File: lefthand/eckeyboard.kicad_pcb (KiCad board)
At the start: 2 copper layers, 135.8 x 94.3 mm, 60 parts, among them J4 Conn_01x06_Male, J5 Conn_01x06_Male, U1 74HC4051, U2 NJM2742, U4 74LS138

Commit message: [add] controller, righthand
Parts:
- TP1, TP10, TP11, TP12, TP13, TP14, TP15, TP16, TP17, TP18, TP19, TP2, TP20, TP21, TP22, TP23, TP24, TP25, TP26, TP27, TP3, TP4, TP5, TP6, TP7, TP8, TP9: value ToprePad -> ToprePad_MntHole; footprint toprepad:ToprePad -> toprepad:ToprePad_MntHole
- moved C7 0.32 mm to (133.3, 129.9)
- moved R15 0.32 mm to (133.3, 131.5)
- moved C6 0.32 mm to (133.3, 126.8)
- moved R14 0.32 mm to (133.3, 128.3)
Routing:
- net GND: track 2927.1 -> 2891.3 mm, vias 9 -> 12
- net /ROW1: track 216.9 -> 227.5 mm
- net /ROW0: track 231.1 -> 238.4 mm
- net /ROW3: track 192.7 -> 199.8 mm
- net /ROW2: track 195.6 -> 198.9 mm
- net /COL3: track 149.5 -> 147.1 mm
- net /MUX_A: track 80.8 -> 82.7 mm
- net /READ: track 97.1 -> 98.3 mm
- net /COL4: track 141.3 -> 140.1 mm
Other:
- board size 135.8 x 94.3 mm -> 137.8 x 98.3 mm

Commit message: [add] step files
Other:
- outline, holes or cut-outs redrawn
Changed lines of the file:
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@@
   (general
     (thickness 1.6)
-    (drawings 47)
+    (drawings 46)
     (tracks 1324)
     (zones 0)
@@
     (arrow2b (pts (xy 31.75 38.95) (xy 32.336421 40.076504)))
   )
-  (gr_line (start 39 137.25) (end 41.05 137.25) (layer Edge.Cuts) (width 0.15))
   (gr_line (start 39 38.95) (end 39 137.25) (layer Edge.Cuts) (width 0.15))
   (gr_line (start 41 38.95) (end 39 38.95) (layer Edge.Cuts) (width 0.15))
@@
   (gr_line (start 176.8 116.65) (end 176.8 116.15) (layer Edge.Cuts) (width 0.15))
   (gr_line (start 167.8 116.65) (end 176.8 116.65) (layer Edge.Cuts) (width 0.15))
-  (gr_line (start 167.8 137.25) (end 41 137.25) (layer Edge.Cuts) (width 0.15))
+  (gr_line (start 167.8 137.25) (end 39 137.25) (layer Edge.Cuts) (width 0.15))
   (gr_line (start 167.8 135.2) (end 167.8 135.25) (layer Edge.Cuts) (width 0.15))
   (gr_line (start 167.8 137.25) (end 167.8 135.2) (layer Edge.Cuts) (width 0.15))

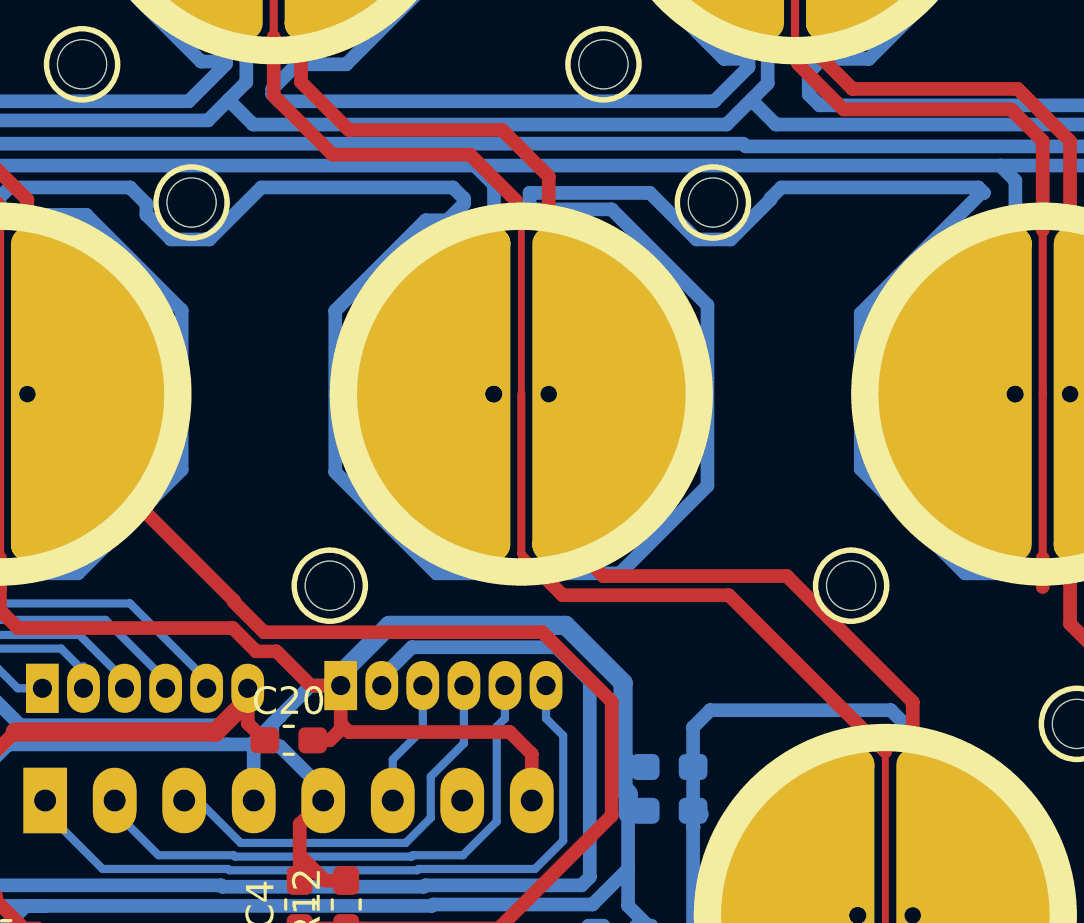
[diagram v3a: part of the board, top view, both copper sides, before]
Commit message: [fix] mounting hole conflict
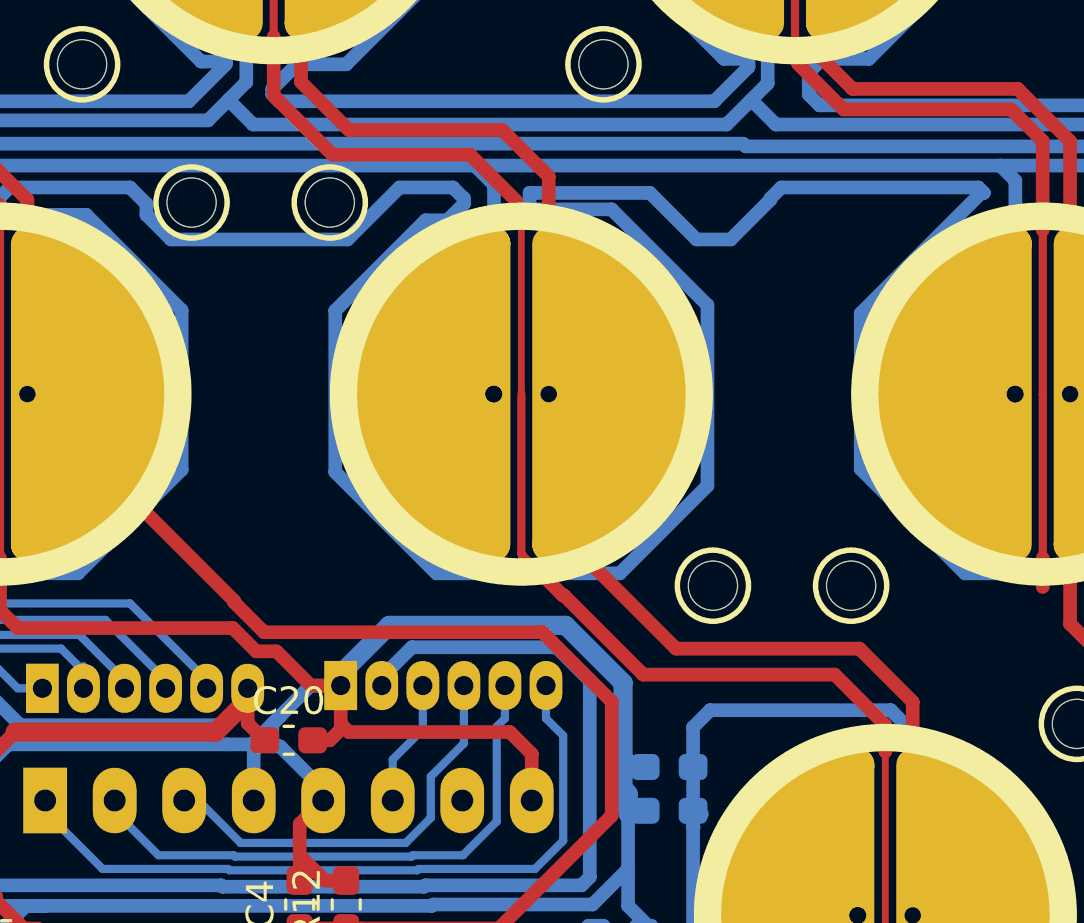
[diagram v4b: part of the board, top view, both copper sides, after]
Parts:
- TP18: value ToprePad_MntHole -> ToprePad_MntHole_B; footprint toprepad:ToprePad_MntHole -> toprepad:ToprePad_MntHole_B
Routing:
- net GND: track 2891.3 -> 2891.9 mm

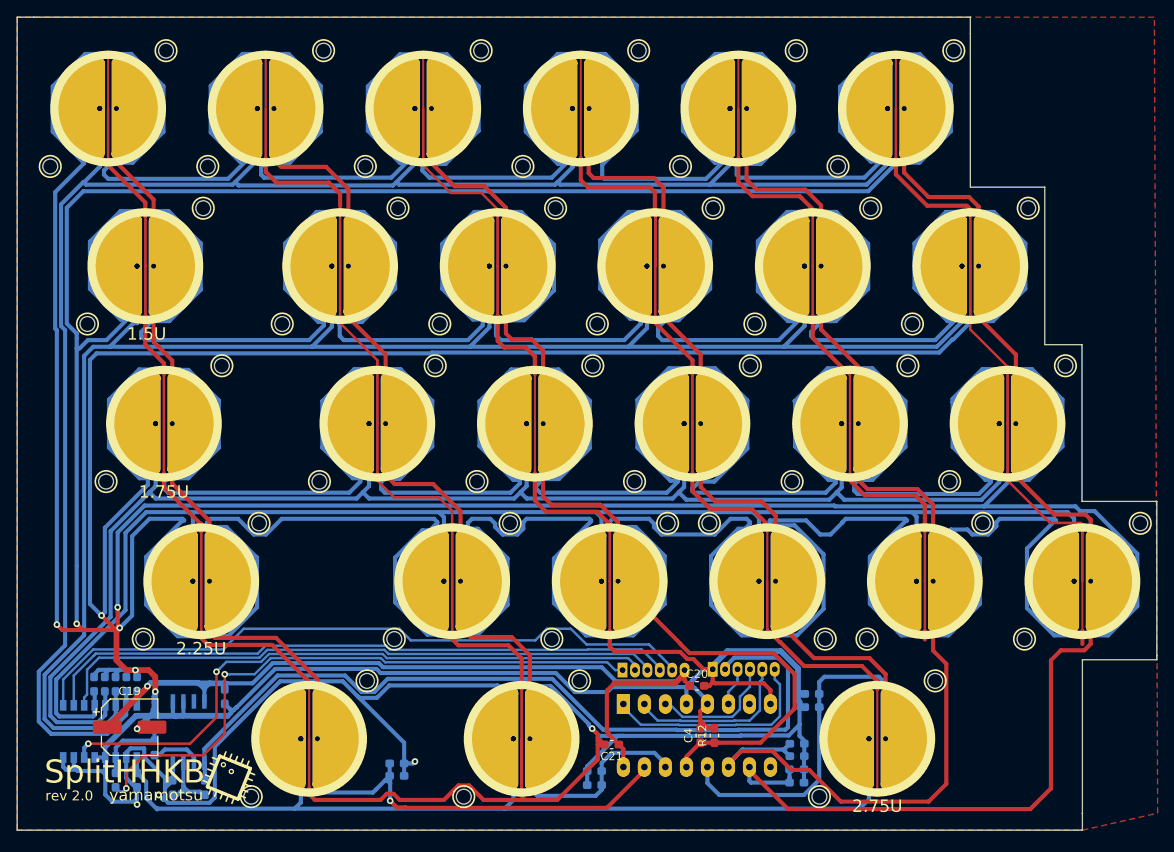
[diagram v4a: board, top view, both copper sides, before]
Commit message: [fix] MUX pin ordering fix
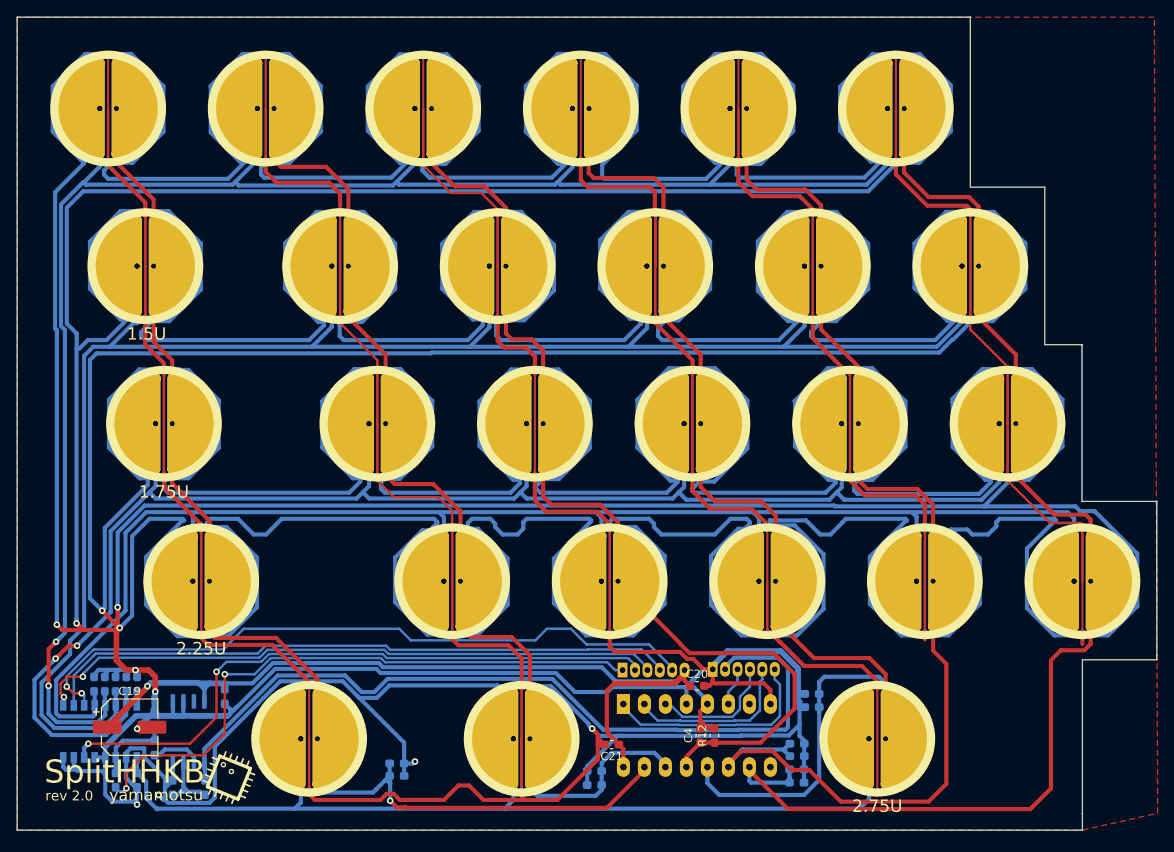
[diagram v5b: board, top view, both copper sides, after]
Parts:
- TP1, TP10, TP11, TP12, TP13, TP14, TP15, TP16, TP17, TP19, TP2, TP20, TP21, TP22, TP23, TP24, TP25, TP26, TP27, TP3, TP4, TP5, TP6, TP7, TP8, TP9: value ToprePad_MntHole -> ToprePad; footprint toprepad:ToprePad_MntHole -> toprepad:ToprePad
- TP18: value ToprePad_MntHole_B -> ToprePad; footprint toprepad:ToprePad_MntHole_B -> toprepad:ToprePad
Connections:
- R1 pad 1: /ROW2 -> /ROW0
- R3 pad 1: /ROW0 -> /ROW2
- U1 pad 11: /MUX_C -> /MUX_A
- U1 pad 13: /ROW2 -> /ROW0
- U1 pad 15: /ROW0 -> /ROW2
- U1 pad 9: /MUX_A -> /MUX_C
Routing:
- net /ROW2: track 198.9 -> 206.1 mm, vias 0 -> 2
- net /ROW0: track 238.4 -> 232.3 mm, vias 0 -> 2
- net /MUX_C: track 74.4 -> 76.9 mm, vias 0 -> 2
- net /MUX_A: track 82.7 -> 84.0 mm, vias 0 -> 2
- net GND: track 2891.9 -> 2891.3 mm

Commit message: [add] lefthand gerber
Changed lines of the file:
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@@
   (general
     (thickness 1.6)
-    (drawings 46)
+    (drawings 59)
     (tracks 1362)
     (zones 0)
@@
   )
   (setup
-    (last_trace_width 0.5)
+    (last_trace_width 0.25)
     (user_trace_width 0.3)
     (user_trace_width 0.5)
@@
       (net 2 GND) (zone_connect 2))
   )
+  (dimension 42.95 (width 0.3) (layer F.Fab)
+    (gr_text "42.950 mm" (at 121.525 154.1) (layer F.Fab)
+      (effects (font (size 1.5 1.5) (thickness 0.3)))
+    )
+    (feature1 (pts (xy 143 126.2) (xy 143 152.586421)))
+    (feature2 (pts (xy 100.05 126.2) (xy 100.05 152.586421)))
+    (crossbar (pts (xy 100.05 152) (xy 143 152)))
+    (arrow1a (pts (xy 143 152) (xy 141.873496 152.586421)))
+    (arrow1b (pts (xy 143 152) (xy 141.873496 151.413579)))
+    (arrow2a (pts (xy 100.05 152) (xy 101.176504 152.586421)))
+    (arrow2b (pts (xy 100.05 152) (xy 101.176504 151.413579)))
+  )
+  (dimension 13.05 (width 0.3) (layer F.Fab)
+    (gr_text "13.050 mm" (at 67.775 141.65) (layer F.Fab)
+      (effects (font (size 1.5 1.5) (thickness 0.3)))
+    )
+    (feature1 (pts (xy 61.25 126.2) (xy 61.25 140.136421)))
+    (feature2 (pts (xy 74.3 126.2) (xy 74.3 140.136421)))
+    (crossbar (pts (xy 74.3 139.55) (xy 61.25 139.55)))
+    (arrow1a (pts (xy 61.25 139.55) (xy 62.376504 138.963579)))
+    (arrow1b (pts (xy 61.25 139.55) (xy 62.376504 140.136421)))
+    (arrow2a (pts (xy 74.3 139.55) (xy 73.173496 138.963579)))
+    (arrow2b (pts (xy 74.3 139.55) (xy 73.173496 140.136421)))
+  )
+  (dimension 35.3 (width 0.3) (layer F.Fab)
+    (gr_text "35.300 mm" (at 56.65 154.15) (layer F.Fab)
+      (effects (font (size 1.5 1.5) (thickness 0.3)))
+    )
+    (feature1 (pts (xy 39 126.2) (xy 39 152.636421)))
+    (feature2 (pts (xy 74.3 126.2) (xy 74.3 152.636421)))
+    (crossbar (pts (xy 74.3 152.05) (xy 39 152.05)))
+    (arrow1a (pts (xy 39 152.05) (xy 40.126504 151.463579)))
+    (arrow1b (pts (xy 39 152.05) (xy 40.126504 152.636421)))
+    (arrow2a (pts (xy 74.3 152.05) (xy 73.173496 151.463579)))
+    (arrow2b (pts (xy 74.3 152.05) (xy 73.173496 152.636421)))
+  )
+  (dimension 11.05 (width 0.3) (layer F.Fab)
+    (gr_text "11.050 mm" (at 26.1 44.475 90) (layer F.Fab)
+      (effects (font (size 1.5 1.5) (thickness 0.3)))
+    )
+    (feature1 (pts (xy 50 38.95) (xy 27.613579 38.95)))
+    (feature2 (pts (xy 50 50) (xy 27.613579 50)))
+    (crossbar (pts (xy 28.2 50) (xy 28.2 38.95)))
+    (arrow1a (pts (xy 28.2 38.95) (xy 28.786421 40.076504)))
+    (arrow1b (pts (xy 28.2 38.95) (xy 27.613579 40.076504)))
+    (arrow2a (pts (xy 28.2 50) (xy 28.786421 48.873496)))
+    (arrow2b (pts (xy 28.2 50) (xy 27.613579 48.873496)))
+  )
+  (dimension 11 (width 0.3) (layer F.Fab)
+    (gr_text "11.000 mm" (at 44.5 54.55) (layer F.Fab)
+      (effects (font (size 1.5 1.5) (thickness 0.3)))
+    )
+    (feature1 (pts (xy 39 50) (xy 39 53.036421)))
+    (feature2 (pts (xy 50 50) (xy 50 53.036421)))
+    (crossbar (pts (xy 50 52.45) (xy 39 52.45)))
+    (arrow1a (pts (xy 39 52.45) (xy 40.126504 51.863579)))
+    (arrow1b (pts (xy 39 52.45) (xy 40.126504 53.036421)))
+    (arrow2a (pts (xy 50 52.45) (xy 48.873496 51.863579)))
+    (arrow2b (pts (xy 50 52.45) (xy 48.873496 53.036421)))
+  )
+  (dimension 25.700049 (width 0.3) (layer F.Fab)
+    (gr_text "25.700 mm" (at 87.204363 154.117602 0.1114702475) (layer F.Fab)
+      (effects (font (size 1.5 1.5) (thickness 0.3)))
+    )
+    (feature1 (pts (xy 100 126.15) (xy 100.051418 152.579026)))
+    (feature2 (pts (xy 74.3 126.2) (xy 74.351418 152.629026)))
+    (crossbar (pts (xy 74.350277 152.042606) (xy 100.050277 151.992606)))
+    (arrow1a (pts (xy 100.050277 151.992606) (xy 98.924916 152.581217)))
+    (arrow1b (pts (xy 100.050277 151.992606) (xy 98.922634 151.408378)))
+    (arrow2a (pts (xy 74.350277 152.042606) (xy 75.47792 152.626834)))
+    (arrow2b (pts (xy 74.350277 152.042606) (xy 75.475638 151.453995)))
+  )
+  (gr_text 1.5U (at 100 136.25) (layer F.SilkS)
+    (effects (font (size 1.5 1.5) (thickness 0.3)))
+  )
+  (dimension 27 (width 0.3) (layer F.Fab)
+    (gr_text "27.000 mm" (at 100 140.8) (layer F.Fab)
+      (effects (font (size 1.5 1.5) (thickness 0.3)))
+    )
+    (feature1 (pts (xy 113.5 135.15) (xy 113.5 139.286421)))
+    (feature2 (pts (xy 86.5 135.15) (xy 86.5 139.286421)))
+    (crossbar (pts (xy 86.5 138.7) (xy 113.5 138.7)))
+    (arrow1a (pts (xy 113.5 138.7) (xy 112.373496 139.286421)))
+    (arrow1b (pts (xy 113.5 138.7) (xy 112.373496 138.113579)))
+    (arrow2a (pts (xy 86.5 138.7) (xy 87.626504 139.286421)))
+    (arrow2b (pts (xy 86.5 138.7) (xy 87.626504 138.113579)))
+  )
+  (gr_line (start 86.5 117.2) (end 100 117.2) (layer F.Fab) (width 0.2))
+  (gr_line (start 86.5 135.2) (end 86.5 117.2) (layer F.Fab) (width 0.2))
+  (gr_line (start 113.5 135.2) (end 86.5 135.2) (layer F.Fab) (width 0.2))
+  (gr_line (start 113.5 117.2) (end 113.5 135.2) (layer F.Fab) (width 0.2))
+  (gr_line (start 100 117.2) (end 113.5 117.2) (layer F.Fab) (width 0.2))
   (dimension 137.8 (width 0.3) (layer F.Fab)
     (gr_text "137.800 mm" (at 107.9 145.7) (layer F.Fab)
